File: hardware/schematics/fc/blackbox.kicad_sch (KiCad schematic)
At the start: 3 parts

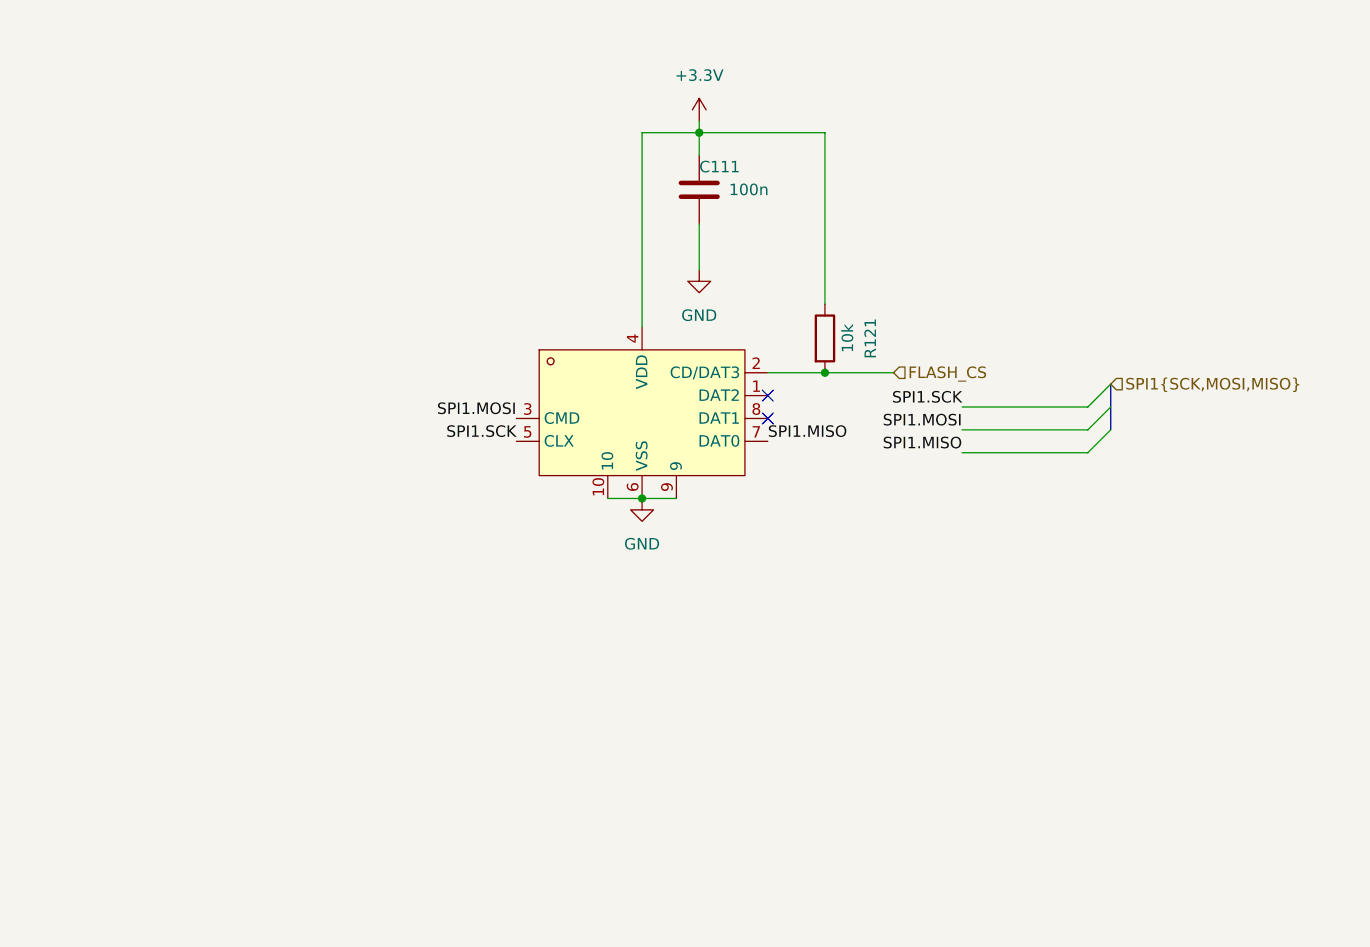
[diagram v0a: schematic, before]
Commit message: Refresh design sources: import rev2 sheets + libs from current sibling repos
FC sheets   <- OpenFC-Lite-Mini rev2 (RP2354A, LMR51430 power tree, COS8051 OSD)
ESC sheets  <- 4in1-mini Rev2 (AT32F421 + NSG2065Q + DOY180N03T, INA186 CSA)
ELRS sheet  <- OpenRX-Lite (ESP32-C3 + SX1281, chip antenna)

Drop-in swaps at paths the root sheet already references; esc_channel
instantiated 4x from root resolves. esc_main.kicad_sch (4in1-mini top:
buck/LDO/CSA/TVS/connector) kept as reference, with ESC.kicad_sch beside
it so its internal channel instances resolve if ever instantiated.

Libraries replaced wholesale: lib(.kicad_sym/.pretty/.3dshapes) from
OpenFC-Lite-Mini, components+4in1ESC from 4in1-mini, OpenRX-Shared from
OpenRX. 3D model paths in OpenRX-Shared.pretty rewritten to project-
local via pcbnew API. Hierarchy verified with kicad-cli netlist export.

Supersedes the 2026-04 port from OpenFC-ECO V0.3 / 4in1ESC 2 (in git
history). Schematic re-annotation + root rewiring is manual work in
KiCad. Old PCB layout retained; footprints are embedded so it opens,
but layout predates this refresh.

Co-Authored-By: Claude Fable 5 <noreply@anthropic.com>
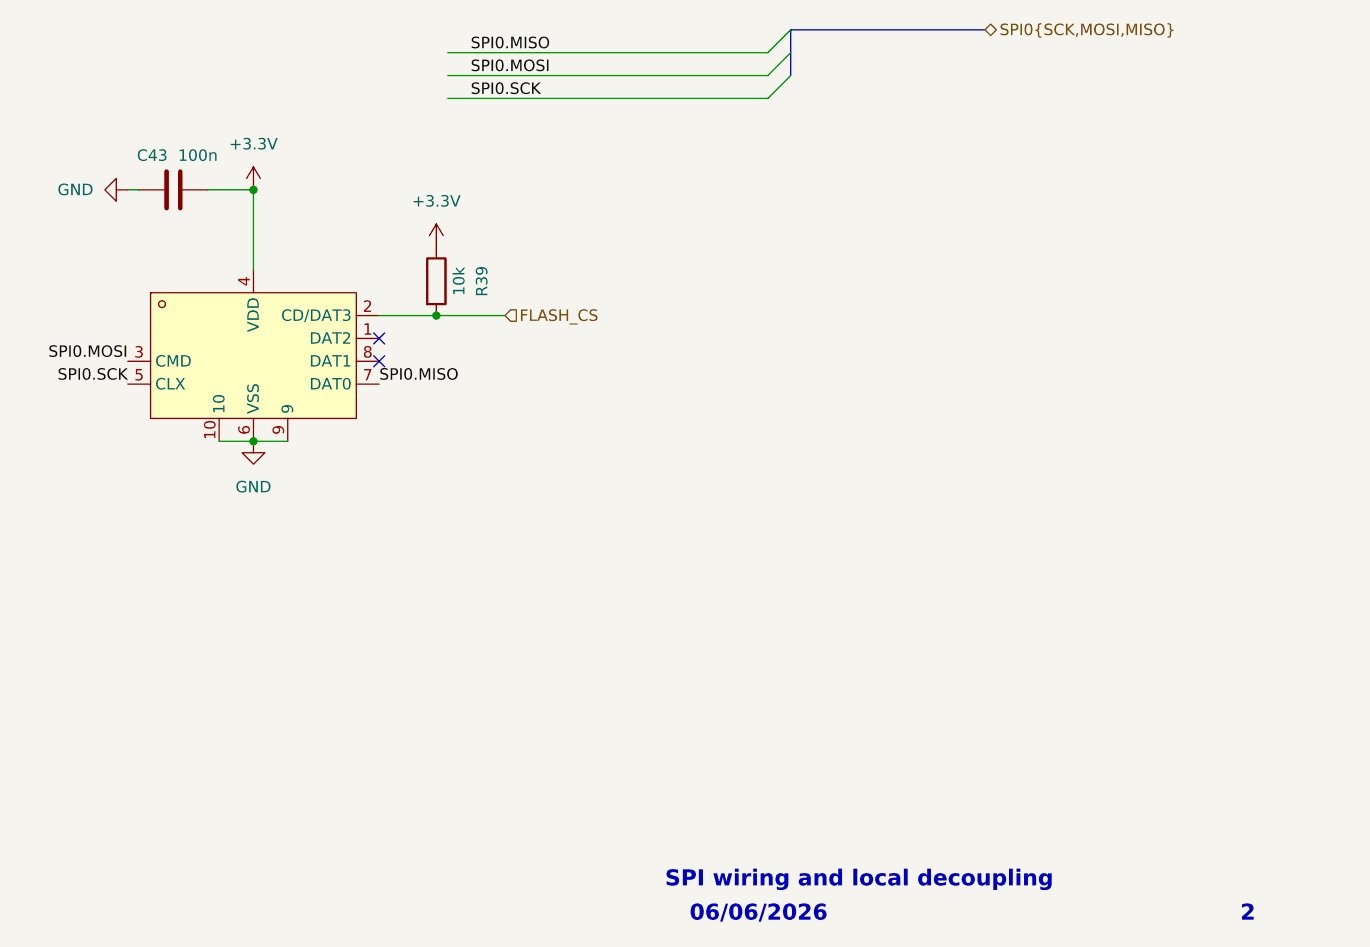
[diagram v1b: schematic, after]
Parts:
- renumbered C111 to C43, R121 to R39
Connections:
- net SPI1.MISO renamed SPI0.MISO
- net SPI1.MOSI renamed SPI0.MOSI
- net SPI1.SCK renamed SPI0.SCK
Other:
- note added: "06/06/2026"
- note added: "2"
- note added: "SPI wiring and local decoupling"
- moved on the sheet: C43, R39
